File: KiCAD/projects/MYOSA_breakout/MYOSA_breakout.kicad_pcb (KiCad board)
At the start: 2 copper layers, 259.6 x 142.8 mm, 26 parts, among them J1 Conn_01x04_Socket, J2 Conn_01x05_Socket, J3 PSU_9V, J4 PSU_GND, Q1 IRLZ44N, SW1 Batt/PSU_switch, SW2 USB/REG_switch, U2 D24V22F5

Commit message: MYOSA PCB v1
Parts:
- removed TP4: 3V3_TestPoint, TestPoint:TestPoint_Pad_2.0x2.0mm
- added ?: , , F.Cu at (101.2, 133.6)
- added ?: , , F.Cu at (101.2, 52.6)
- added ?: , , F.Cu at (187.2, 133.3)
- added REF**: MountingHole_2.1mm, MountingHole:MountingHole_2.1mm, F.Cu at (187.2, 52.6)
- BT1, J3, J4: moved to B.Cu
- TP1, TP3, TP5, TP6: footprint TestPoint:TestPoint_Pad_2.0x2.0mm -> TestPoint:TestPoint_Loop_D2.50mm_Drill1.85mm
- moved U2 129.3 mm to (176.5, 108.5), turned to -90 degrees
- moved R_reg_LED1 124.4 mm to (165.9, 116.8), turned to -90 degrees
- moved R_ADC_pulldown1 118.8 mm to (159.9, 101.6), turned to 90 degrees
- moved C_Vin1 112.5 mm to (155.3, 125.4), turned to 180 degrees
- moved R_Vin1 107.0 mm to (146.0, 125.5), turned to 180 degrees
- moved C_ADC_cap1 104.7 mm to (155.7, 101.5), turned to 90 degrees
- moved 5V_Reg_LED1 101.4 mm to (182.8, 116.7), turned to 180 degrees
- moved BT1 92.4 mm to (140.5, 120.6), turned to 90 degrees
- moved TP6 79.7 mm to (124.5, 126.6)
- moved Q1 79.1 mm to (105.3, 115.5), turned to 90 degrees
- moved TP3 78.8 mm to (118.8, 126.8)
- moved R_FET_pulldown1 78.6 mm to (115.0, 116.7), turned to 90 degrees
- moved SW_BAT/PSU1 74.2 mm to (149.3, 113.3), turned to 180 degrees
- moved R_FET_Gate1 72.8 mm to (110.4, 109.0), turned to -90 degrees
- moved R_series_MWIR_LED1 72.0 mm to (117.4, 81.8), turned to 90 degrees
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- renumbered D1 to 5V_Reg_LED1, J1 to CON_BMP180_1, J2 to CON_LED_Photodiode1, C2 to C_3V3_out1, ADC_cap1 to C_ADC_cap1, C1 to C_Vin1, ADC_pulldown1 to R_ADC_pulldown1, R2 to R_FET_Gate1, R3 to R_FET_pulldown1, R5 to R_Vin1, R4 to R_reg_LED1, R1 to R_series_MWIR_LED1, SW1 to SW_BAT/PSU1, SW2 to SW_USB1
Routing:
- net /5V: track 0.00 -> 115.8 mm, vias 0 -> 2
- net /Photo_IN: track 0.00 -> 107.1 mm, vias 0 -> 2
- net /LED_Anode: track 0.00 -> 58.4 mm, vias 0 -> 1
- net /CLK: track 0.00 -> 53.5 mm, vias 0 -> 2
- net /PWM: track 0.00 -> 53.5 mm
- net /3V3_OUT: track 0.00 -> 49.8 mm
- net /DAT: track 0.00 -> 46.5 mm, vias 0 -> 2
- net Net-(J3-Pin_1): track 0.00 -> 46.1 mm
- net /LED_Cathode: track 0.00 -> 43.5 mm
- net /Vin_SRC: track 0.00 -> 26.5 mm
- net Net-(Q1-G): track 0.00 -> 21.3 mm
- net Net-(5V_Reg_LED1-A): track 0.00 -> 20.4 mm
- net Net-(SW_USB1-C): track 0.00 -> 14.8 mm
- net Net-(BT1-+): track 0.00 -> 9.36 mm
- net Net-(C_Vin1-Pad2): track 0.00 -> 4.27 mm
- added copper zone on B.Cu, net GND
- added copper zone on F.Cu, net GND
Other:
- board size 259.6 x 142.8 mm -> 94.3 x 87.4 mm
- board text added: "+-"
- board text added: "100"
- board text added: "100k"
- board text added: "100n"
- board text added: "1k"
- board text added: "200"
- board text added: "3R4"
- board text added: "3V3"
- board text added: "5V"
- board text added: "CLK"
- board text added: "DAT"
- board text added: "DAT x x CLK x"
- board text added: "GND"
- board text added: "LED+"
- board text added: "LED-"
- board text added: "MYOSA USB|VIN"
- board text added: "PERIPH. BAT|PSU"
- board text added: "PWM"
- board text added: "Photo"
- board text added: "v"

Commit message: KiCAD Updates + Manufacturing
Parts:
- removed ? (x3): , 
- removed CON_BMP180_1: Conn_01x04_Socket, Connector_JST:JST_EH_S4B-EH_1x04_P2.50mm_Horizontal
- removed REF**: MountingHole_2.1mm, MountingHole:MountingHole_2.1mm
- J3: footprint Connector:Banana_Cliff_FCR7350R_S16N-PC_Horizontal -> Connector:Banana_Jack_1Pin
- J4: footprint Connector:Banana_Cliff_FCR7350B_S16N-PC_Horizontal -> Connector:Banana_Jack_1Pin
- SW_BAT/PSU1, SW_USB1: footprint Button_Switch_THT:SW_Slide_SPDT_Straight_CK_OS102011MS2Q -> Button_Switch_THT:SW_Slide-03_Wuerth-WS-SLTV_10x2.5x6.4_P2.54mm
- moved BT1 20.8 mm to (119.7, 122.5), turned to 0 degrees
- moved J3 18.7 mm to (175.5, 90.8)
- moved J4 16.2 mm to (175.6, 69.5)
- moved R_series_MWIR_LED1 11.9 mm to (129.1, 83.7), turned to 180 degrees
- moved CON_LED_Photodiode1 10.2 mm to (113.7, 86.8)
- moved SW_BAT/PSU1 1.85 mm to (147.5, 112.9)
- moved 5V_Reg_LED1 0.91 mm to (181.9, 116.6)
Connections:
- U1 pad 15: /CLK -> unconnected-(U1-SCL-Pad15)
- U1 pad 18: /DAT -> unconnected-(U1-SDA-Pad18)
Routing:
- net /CLK: track 53.5 -> 0.00 mm, vias 2 -> 0
- net /DAT: track 46.5 -> 0.00 mm, vias 2 -> 0
- net /3V3_OUT: track 49.8 -> 33.4 mm
- net Net-(J3-Pin_1): track 46.1 -> 34.7 mm
- net /LED_Anode: track 58.4 -> 47.3 mm
- net /LED_Cathode: track 43.5 -> 34.1 mm
- net /Photo_IN: track 107.1 -> 112.2 mm
- net Net-(5V_Reg_LED1-A): track 20.4 -> 16.7 mm
- net /5V: track 115.8 -> 118.9 mm, vias 2 -> 0
- net Net-(BT1-+): track 9.36 -> 7.73 mm, vias 0 -> 1
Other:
- board size 94.3 x 87.4 mm -> 88.9 x 78.2 mm
- board text added: "MYOSA VIN|USB"
- board text removed: "CLK"
- board text removed: "DAT"
- board text removed: "DAT x x CLK x"
- board text removed: "MYOSA USB|VIN"

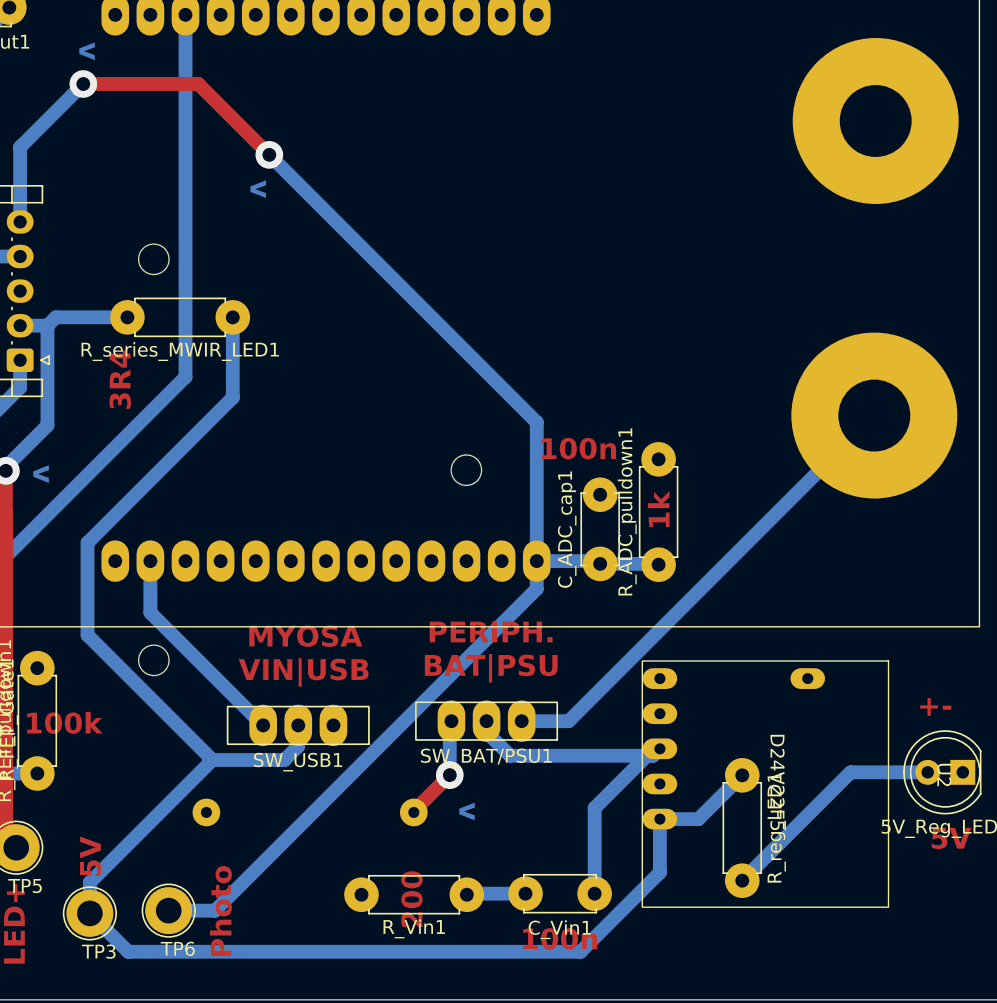
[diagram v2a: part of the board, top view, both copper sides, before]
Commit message: Change pad properties of banana plugs and battery holder to be larger
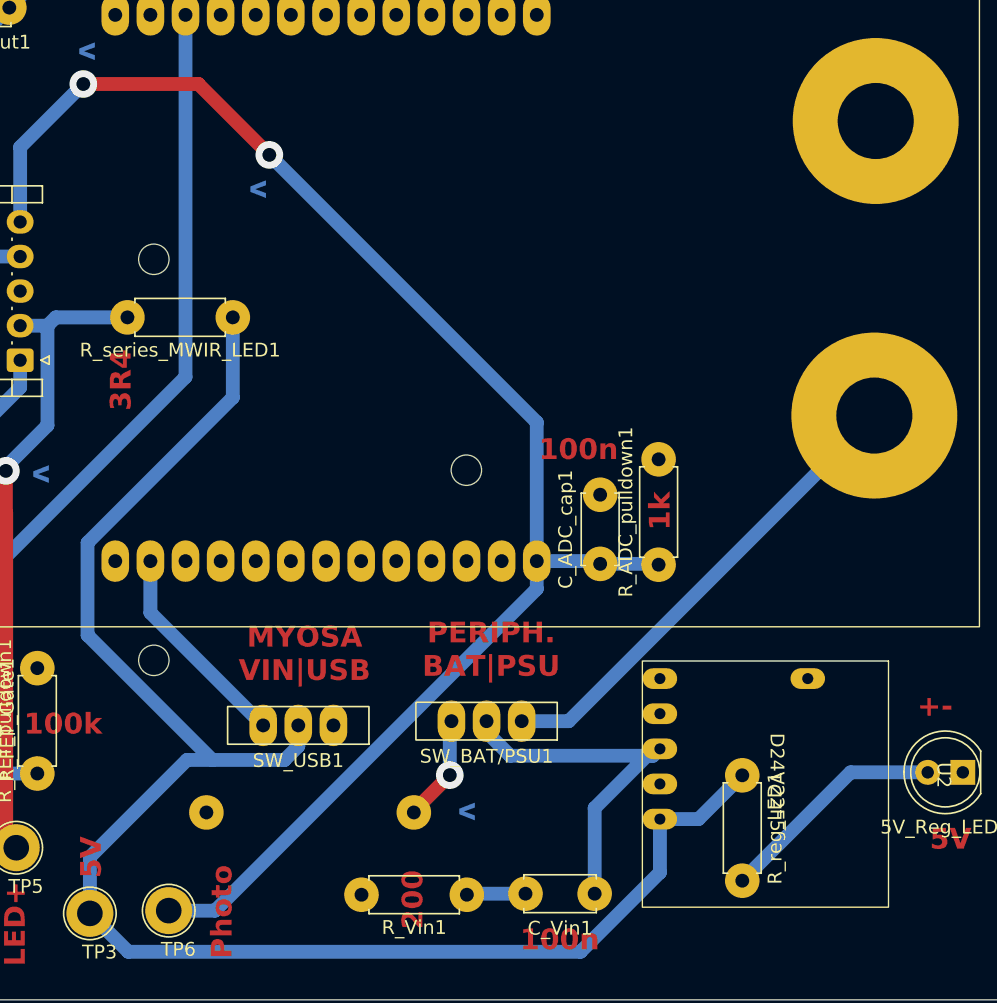
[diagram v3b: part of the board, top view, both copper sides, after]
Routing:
- net /5V: track 118.9 -> 119.9 mm
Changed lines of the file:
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@@
 			(at 0 0 180)
 			(size 12 12)
-			(drill 5.2)
+			(drill 5.5)
 			(layers "*.Cu" "*.Mask")
 			(remove_unused_layers no)
@@
 			(at 0 0 180)
 			(size 12 12)
-			(drill 5.2)
+			(drill 5.5)
 			(layers "*.Cu" "*.Mask")
 			(remove_unused_layers no)
@@
 		(pad "1" thru_hole circle
 			(at 22.5 -3)
-			(size 2 2)
-			(drill 0.8)
+			(size 2.5 2.5)
+			(drill 1)
 			(layers "*.Cu" "*.Mask")
 			(remove_unused_layers no)
@@
 		(pad "2" thru_hole circle
 			(at 7.5 -3)
-			(size 2 2)
-			(drill 0.8)
+			(size 2.5 2.5)
+			(drill 1)
 			(layers "*.Cu" "*.Mask")
 			(remove_unused_layers no)
@@
 	)
 	(segment
+		(start 125.793506 115.706494)
+		(end 127.635231 115.706494)
+		(width 1)
+		(layer "B.Cu")
+		(net 9)
+	)
+	(segment
 		(start 118.609 99.996159)
 		(end 118.609 106.680263)
@@
 	)
 	(segment
-		(start 118.775 124.566725)
-		(end 127.635231 115.706494)
-		(width 1)
-		(layer "B.Cu")
-		(net 9)
-	)
-	(segment
 		(start 159.995 119.98)
 		(end 162.785 119.98)
@@
 	(segment
 		(start 118.775 126.8)
-		(end 118.775 124.566725)
+		(end 118.775 122.725)
 		(width 1)
 		(layer "B.Cu")
@@
 		(width 1)
 		(layer "B.Cu")
+		(net 9)
+	)
+	(segment
+		(start 118.775 122.725)
+		(end 125.793506 115.706494)
+		(width 1)
+		(layer "B.Cu")

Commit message: Increase pad size of hardware connector
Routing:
- net /LED_Anode: track 47.3 -> 48.8 mm
- net /3V3_OUT: track 33.4 -> 34.4 mm
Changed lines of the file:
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@@
 			)
 		)
-		(pad "1" thru_hole roundrect
+		(pad "1" thru_hole oval
 			(at 0 0 90)
-			(size 1.7 1.95)
-			(drill 0.95)
+			(size 2 3)
+			(drill 1)
 			(layers "*.Cu" "*.Mask")
 			(remove_unused_layers no)
-			(roundrect_rratio 0.147059)
 			(net 7 "/LED_Cathode")
 			(pinfunction "Pin_1")
@@
 		(pad "2" thru_hole oval
 			(at 2.5 0 90)
-			(size 1.7 1.95)
-			(drill 0.95)
+			(size 2 3)
+			(drill 1)
 			(layers "*.Cu" "*.Mask")
 			(remove_unused_layers no)
@@
 		(pad "3" thru_hole oval
 			(at 5 0 90)
-			(size 1.7 1.95)
-			(drill 0.95)
+			(size 2 3)
+			(drill 1)
 			(layers "*.Cu" "*.Mask")
 			(remove_unused_layers no)
@@
 		(pad "4" thru_hole oval
 			(at 7.5 0 90)
-			(size 1.7 1.95)
-			(drill 0.95)
+			(size 2 3)
+			(drill 1)
 			(layers "*.Cu" "*.Mask")
 			(remove_unused_layers no)
@@
 		(pad "5" thru_hole oval
 			(at 10 0 90)
-			(size 1.7 1.95)
-			(drill 0.95)
+			(size 2 3)
+			(drill 1)
 			(layers "*.Cu" "*.Mask")
 			(remove_unused_layers no)
@@
 	)
 	(segment
-		(start 111.7565 79.299)
-		(end 111.7565 62.4935)
+		(start 110.5 63.75)
+		(end 112.95 61.3)
+		(width 1)
+		(layer "B.Cu")
+		(net 5)
+	)
+	(segment
+		(start 110.5 78.0425)
+		(end 110.5 63.75)
 		(width 1)
 		(layer "B.Cu")
@@
 	)
 	(segment
-		(start 111.7575 79.3)
-		(end 111.7565 79.299)
-		(width 1)
-		(layer "B.Cu")
-		(net 5)
-	)
-	(segment
 		(start 113.7325 79.3)
 		(end 111.7575 79.3)
@@
 	)
 	(segment
+		(start 111.7575 79.3)
+		(end 110.5 78.0425)
+		(width 1)
+		(layer "B.Cu")
+		(net 5)
+	)
+	(segment
 		(start 122.149 59.324)
 		(end 123.15 60.325)
-		(width 1)
-		(layer "B.Cu")
-		(net 5)
-	)
-	(segment
-		(start 111.7565 62.4935)
-		(end 112.95 61.3)
 		(width 1)
 		(layer "B.Cu")
@@
 	)
 	(segment
+		(start 112.7 94.8)
+		(end 112.7 94.521675)
+		(width 1)
+		(layer "B.Cu")
+		(net 8)
+	)
+	(segment
 		(start 116.3075 83.7)
 		(end 121.49 83.7)
@@
 	)
 	(segment
-		(start 115.7085 91.513175)
-		(end 115.7085 84.301)
+		(start 112.7 94.521675)
+		(end 117.5 89.721675)
+		(width 1)
+		(layer "B.Cu")
+		(net 8)
+	)
+	(segment
+		(start 117.5 86.0925)
+		(end 115.7075 84.3)
 		(width 1)
 		(layer "B.Cu")
@@
 	)
 	(segment
-		(start 115.7085 84.301)
-		(end 115.7075 84.3)
-		(width 1)
-		(layer "B.Cu")
-		(net 8)
-	)
-	(segment
-		(start 112.7 94.8)
-		(end 112.7 94.521675)
-		(width 1)
-		(layer "B.Cu")
-		(net 8)
-	)
-	(segment
-		(start 112.7 94.521675)
-		(end 115.7085 91.513175)
-		(width 1)
-		(layer "B.Cu")
+		(start 117.5 89.721675)
+		(end 117.5 86.0925)
+		(width 1)
+		(layer "B.Cu")
